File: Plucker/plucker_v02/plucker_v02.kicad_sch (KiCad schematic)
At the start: 10 parts, among them J1_BNC1 BNC5-J-P-GN-RA-BH2D, J2_BLACK1 Conn_01x01, J3_RED1 Conn_01x01, T1 GT07-110-013, U1 SL1002A600SP

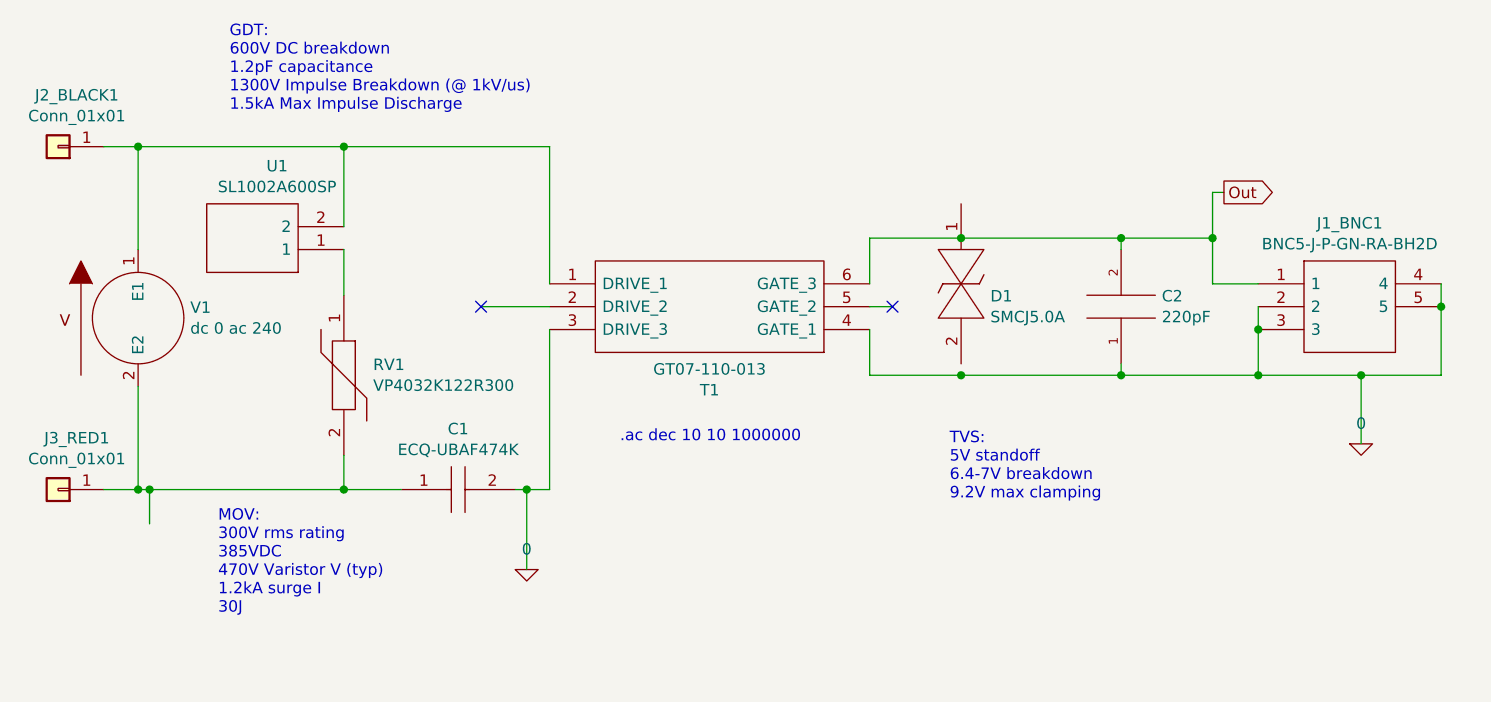
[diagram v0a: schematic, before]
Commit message: Added Pulse Proof Resistor
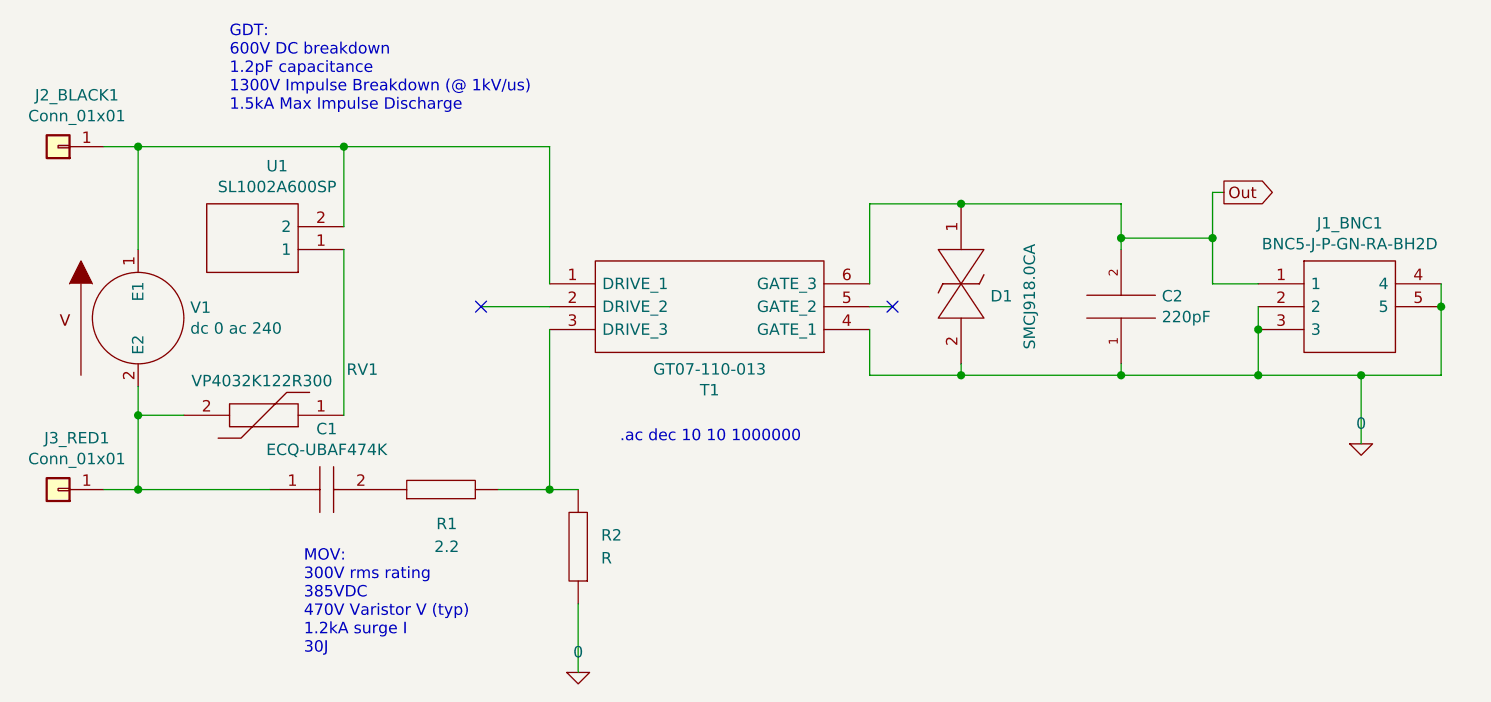
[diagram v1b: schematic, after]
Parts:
- added R1: 2.2, Resistor_SMD:R_2010_5025Metric_Pad1.40x2.65mm_HandSolder, symbol pspice:R
- added R2: R, symbol pspice:R
- D1: value SMCJ5.0A -> SMCJ918.0CA; footprint DIONM7959X262N -> kyuditsky_kicad:littlefuseTVS; Spice_Lib_File /Users/MacMini/Documents/KiCad/HPF/HPF_SPICE/SMCJ5.0A_spice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 -> /Users/mac/Documents/KiCad/6.0/projects/HPF/HPF_SPICE/SMCJ5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; Spice_Netlist_Enabled Y -> N
- J1_BNC1: footprint BNC5JPGNRABH2D -> kyuditsky_kicad:BNC5JPGNRABH2D
- J2_BLACK1, J3_RED1: footprint Connector_Coaxial:SMA_Amphenol_132203-12_Horizontal -> kyuditsky_kicad:Banana_Jack_S_RA_73099
- RV1: footprint CAPPM10080X500N -> kyuditsky_kicad:MOV_VP4032K122R300; Spice_Netlist_Enabled Y -> N
- T1: Spice_Lib_File /Users/MacMini/Documents/KiCad/HPF/HPF_SPICE/GTRANS_01.lib -> /Users/mac/Documents/KiCad/6.0/projects/HPF/HPF_SPICE/GTRAN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
- U1: footprint SL1002A600SP -> kyuditsky_kicad:SL1002A600SP; Spice_Netlist_Enabled Y -> N
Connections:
- net 0: now also D1.2, R2.1; no longer C1.2, T1.3 (DRIVE_3)
- net Out: now also D1.1
- new net: C1.2, R1.1
- new net: R1.2, R2.2, T1.3 (DRIVE_3)
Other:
- note removed: "TVS: 5V standoff 6.4-7V breakdown 9.2V max clamping"
- moved on the sheet: C1, RV1
